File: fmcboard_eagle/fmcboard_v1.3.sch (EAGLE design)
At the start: 128 parts, among them IC1 OPA699ID, IC10 LTC6229IMS8E#TRPBF, IC11 7805TV, IC12 7905, IC3 LTC6229IMS8E#TRPBF, IC4 LTC6229IMS8E#TRPBF, IC5 LM358, IC6 OPA699ID, IC7 OPA699ID, IC8 LTC6229IMS8E#TRPBF, IC9 LTC6229IMS8E#TRPBF, J1 8pin, J12 4p-2.54, J2 ASP-134604-01, J3 4p-2.54, J4 4p-2.54, J5 8pin, J6 4p-2.54, J7 4p-2.54, J8 4p-2.54, U1 TXS0108EPWR

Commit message: v1.3
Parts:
- R42: value 50 -> 50?
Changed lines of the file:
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@@
 <part name="C33" library="SparkFun-Passives" deviceset="CAP" device="0805" value="1pF"/>
 <part name="R34" library="rcl" library_urn="urn:adsk.eagle:library:334" deviceset="R-US_" device="R0805" package3d_urn="urn:adsk.eagle:package:23553/2" value="50"/>
-<part name="R42" library="rcl" library_urn="urn:adsk.eagle:library:334" deviceset="R-US_" device="R0805" package3d_urn="urn:adsk.eagle:package:23553/2" value="50"/>
+<part name="R42" library="rcl" library_urn="urn:adsk.eagle:library:334" deviceset="R-US_" device="R0805" package3d_urn="urn:adsk.eagle:package:23553/2" value="50?"/>
 <part name="J8" library="Seeed-Connector" library_urn="urn:adsk.eagle:library:478" deviceset="DIP-BLACK-FEMALE-HEADER-VERT(4P-2.54)" device="" package3d_urn="urn:adsk.eagle:package:33137/1" value="4p-2.54"/>
 <part name="IC11" library="linear" library_urn="urn:adsk.eagle:library:262" deviceset="78*" device="TV" package3d_urn="urn:adsk.eagle:package:16417/2" technology="05"/>

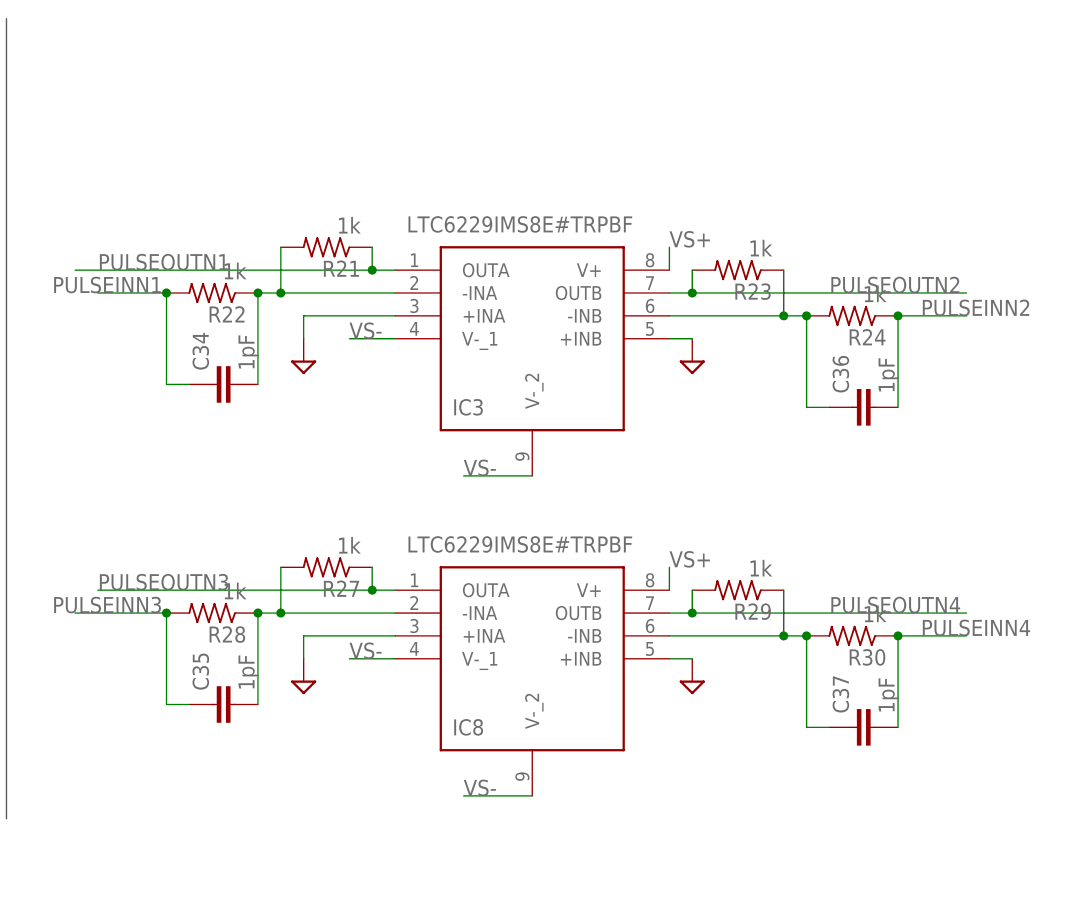
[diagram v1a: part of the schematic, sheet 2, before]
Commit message: Fix feedback compensation caps on neg pulse amps, new footprint for L7905
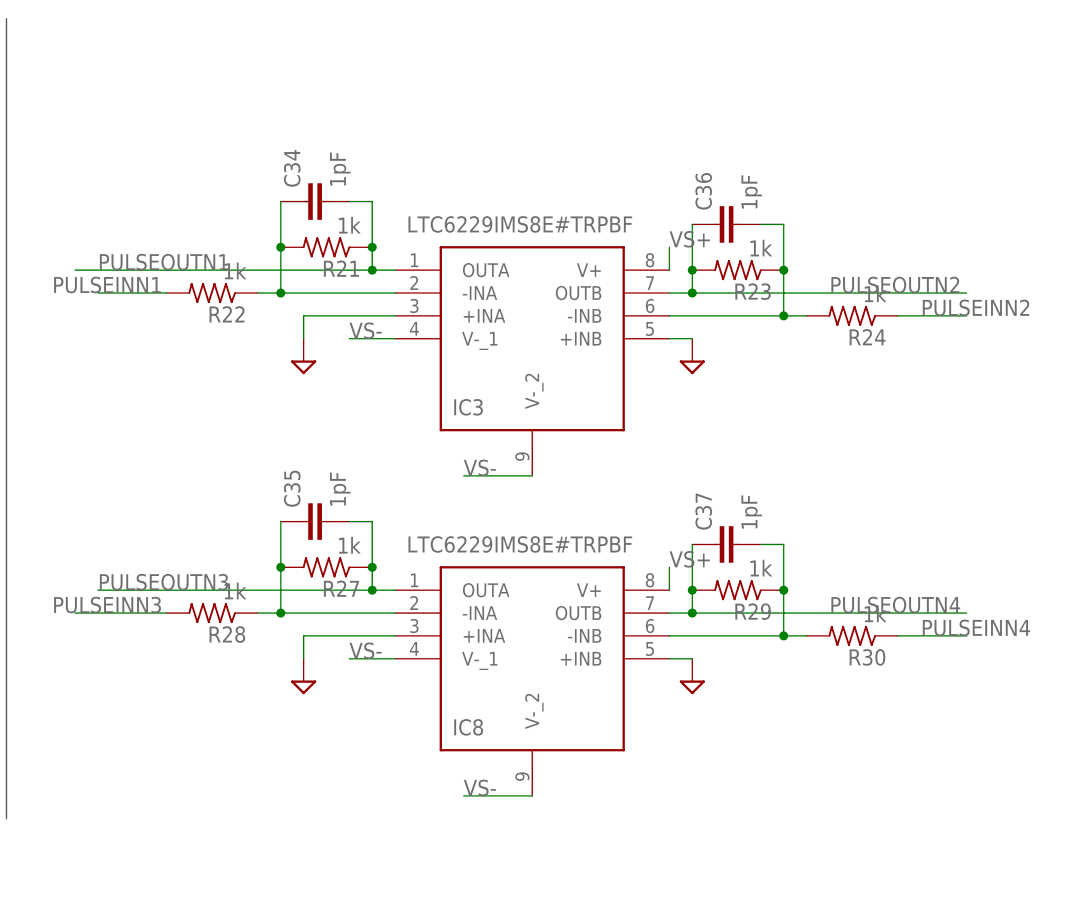
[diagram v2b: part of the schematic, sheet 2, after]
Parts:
- removed IC12: 7905, linear:7905T
- added U2: STMICROELECTRONICS_L7905ACVSTMICROELECTRONICS_L7905ACV_0_0, STMicroelectronics - L7905ACV:STMICROELECTRONICS_L7905ACVSTMICROELECTRONICS_L7905ACV_0_0
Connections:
- net GND: now also U2.GND; no longer IC12.GND
- net N$12: now also C35.1; no longer C35.2
- net N$13: now also C34.1; no longer C34.2
- net N$14: now also C37.2; no longer C37.1
- net N$4: now also C36.2; no longer C36.1
- net PULSEINN1: no longer C34.1
- net PULSEINN2: no longer C36.2
- net PULSEINN3: no longer C35.1
- net PULSEINN4: no longer C37.2
- net PULSEOUTN1: now also C34.2
- net PULSEOUTN2: now also C36.1
- net PULSEOUTN3: now also C35.2
- net PULSEOUTN4: now also C37.1
- net VIN-CLEAN: now also U2.IN; no longer IC12.VI
- net VS-: now also U2.OUT; no longer IC12.VO
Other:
- moved on the sheet: C34, C35, C36, C37
